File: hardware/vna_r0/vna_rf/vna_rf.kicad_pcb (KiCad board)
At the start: 2 copper layers, 122 parts, among them J401 CONN_02X10, U201 LMX2594, U202 LTC2630, U203 ADRF5040, U204 LTC2054CS5, U205 MAAM-011100, U301 NC7WZU04, U302 PE42521, U303 MASW-008322-TR1000, U304 PE42521, U401 CONN_SMA_2GND, U402 CONN_SMA_2GND, U403 CONN_SMA

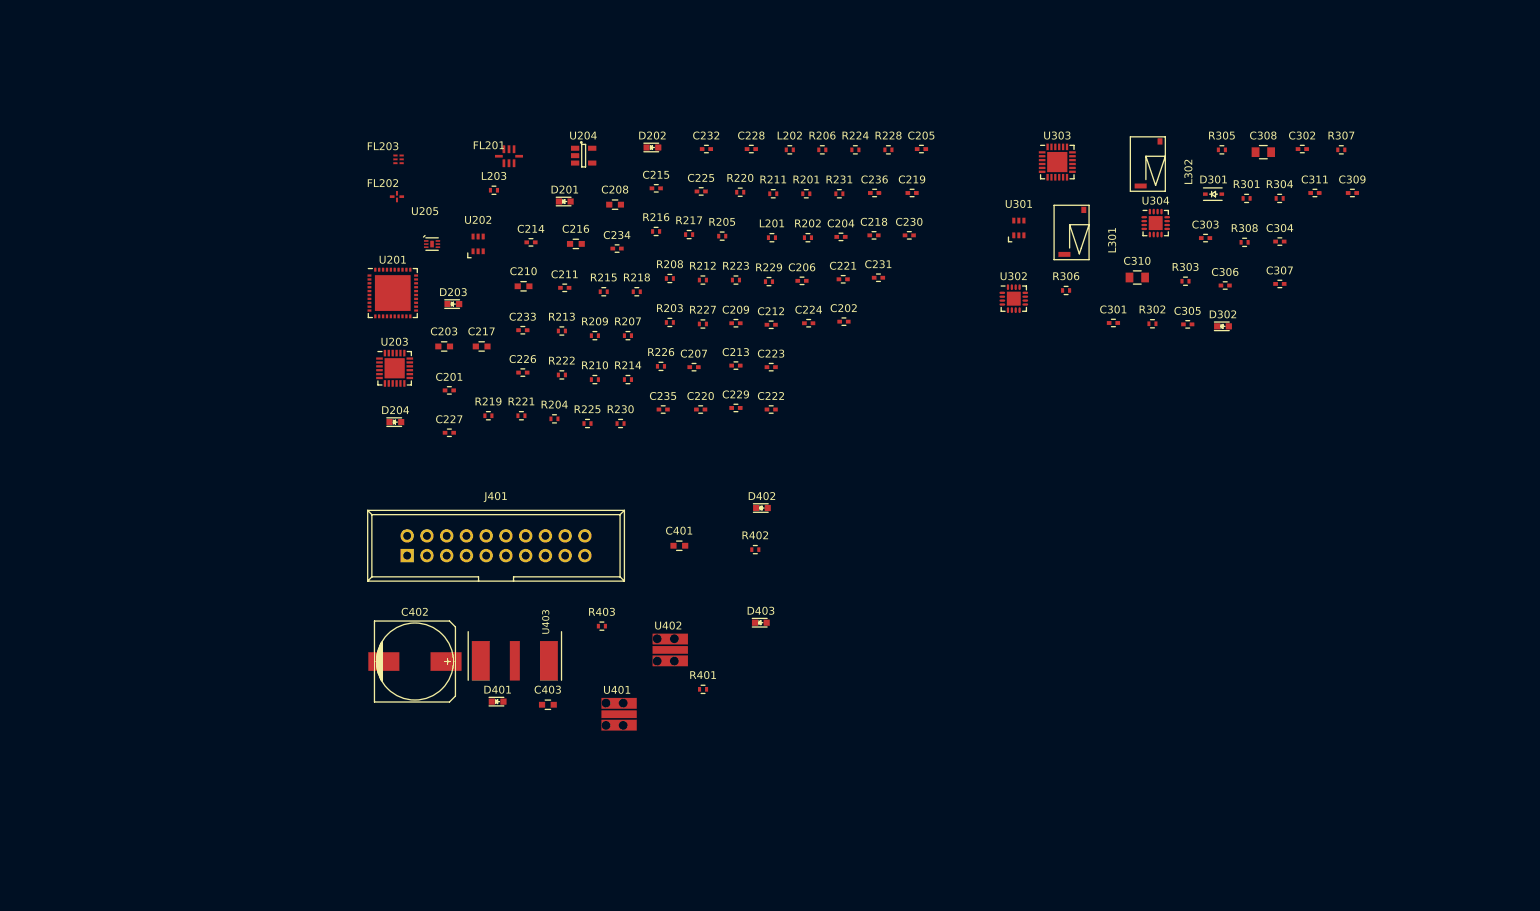
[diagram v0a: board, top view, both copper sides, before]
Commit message: work on vna r0 component placement
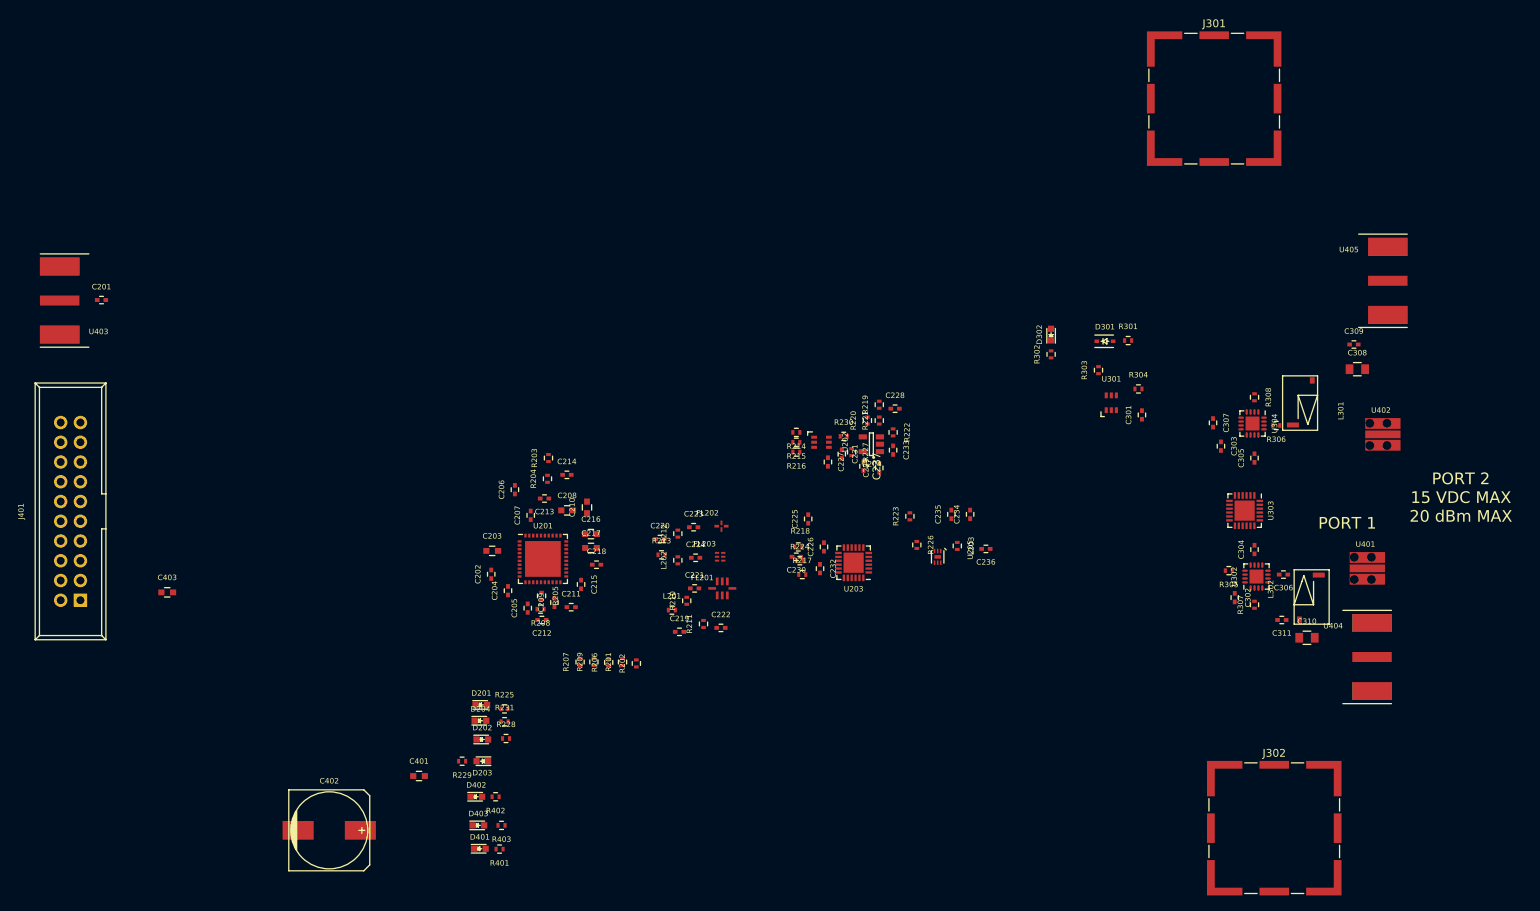
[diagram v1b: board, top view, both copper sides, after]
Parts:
- added C237: 100 nF, Capacitors_SMD:C_0402, F.Cu at (187.5, 95.5)
- added J301: RF_Shield_Two_Pieces, Shielding_Cabinets:Laird_Technologies_BMI-S-202-F_16.50x16.50mm, F.Cu at (232.6, 48.3)
- added J302: RF_Shield_Two_Pieces, Shielding_Cabinets:Laird_Technologies_BMI-S-202-F_16.50x16.50mm, F.Cu at (240.3, 142.1)
- added U404: CONN_SMA, vna_footprints:732511150_sma_thin, F.Cu at (252.9, 120.1)
- added U405: CONN_SMA, vna_footprints:732511150_sma_thin, F.Cu at (254.9, 71.7)
- moved U401 98.0 mm to (252.3, 108.7)
- moved U402 95.8 mm to (254.3, 91.4)
- moved R228 90.3 mm to (141.5, 130.6)
- moved R231 80.4 mm to (141.3, 128.4)
- moved D202 79.2 mm to (138.4, 130.7)
- moved C205 77.8 mm to (144.3, 113.8), turned to 90 degrees
- moved U205 76.5 mm to (197.0, 107.2), turned to 270 degrees
- moved L203 75.1 mm to (199.5, 105.8), turned to 270 degrees
- moved U403 74.7 mm to (84.1, 74.2), turned to 270 degrees
- moved R229 73.2 mm to (135.8, 133.5), turned to 180 degrees
- moved R206 71.4 mm to (154.7, 120.8), turned to 90 degrees
- moved FL203 65.8 mm to (169.0, 107.2)
- moved D201 65.6 mm to (138.3, 126.2)
- moved R201 64.7 mm to (156.5, 120.7), turned to 90 degrees
- moved U203 64.1 mm to (186.2, 108.0), turned to 180 degrees
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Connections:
- net /port_switch/PORT1_BIAS renamed /PORT1_BIAS
- net /port_switch/PORT2_BIAS renamed /PORT2_BIAS
- C304 pad 1: Net-(C304-Pad1) -> /conn_power/PORT1
- R307 pad 1: Net-(R307-Pad1) -> GND
- R307 pad 2: GND -> Net-(R307-Pad2)
- U302 pad 11: Net-(R307-Pad1) -> /conn_power/PORT1
- U302 pad 15: +3V3 -> GND
- U302 pad 2: Net-(C304-Pad1) -> Net-(R307-Pad2)
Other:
- copper layers 2 -> 4
- board text added: "PORT 1"
- board text added: "PORT 2 15 VDC MAX 20 dBm MAX"

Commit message: work on vna r0 layout..
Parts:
- added H401: MOUNTING_HOLE, Mounting_Holes:MountingHole_2-7mm, F.Cu at (192.9, 79.1)
- added H402: MOUNTING_HOLE, Mounting_Holes:MountingHole_2-7mm, F.Cu at (251.0, 120.8)
- added H403: MOUNTING_HOLE, Mounting_Holes:MountingHole_2-7mm, F.Cu at (174.1, 124.1)
- added H404: MOUNTING_HOLE, Mounting_Holes:MountingHole_2-7mm, F.Cu at (251.0, 79.9)
- added J402: RF_Shield_Two_Pieces, Shielding_Cabinets:Laird_Technologies_BMI-S-205-F_38.10x25.40mm, F.Cu at (146.5, 96.6)
- moved U403 92.4 mm to (176.3, 79.2), turned to 180 degrees
- moved C201 87.6 mm to (176.4, 84.6), turned to 270 degrees
- moved J401 85.7 mm to (172.5, 114.3)
- moved C403 81.3 mm to (178.9, 104.6)
- moved C402 75.7 mm to (190.6, 118.5)
- moved D401 62.6 mm to (199.8, 134.2), turned to 90 degrees
- moved R401 60.7 mm to (199.9, 131.6), turned to 270 degrees
- moved D403 59.4 mm to (196.8, 134.3), turned to 90 degrees
- moved C401 58.5 mm to (188.6, 130.6), turned to 90 degrees
- moved R403 56.9 mm to (196.8, 131.4), turned to 270 degrees
- moved D402 55.6 mm to (193.1, 134.6), turned to 90 degrees
- moved D302 53.9 mm to (205.6, 132.2)
- moved R302 53.9 mm to (205.6, 134.7)
- moved R402 53.3 mm to (193.1, 132.1), turned to 270 degrees
- moved R229 52.8 mm to (188.6, 136.4), turned to 270 degrees
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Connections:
- C222 pad 2: /rf_synth/RF_4 -> /rf_synth/RF_1
- C304 pad 1: /conn_power/PORT1 -> Net-(C304-Pad1)
- FL202 pad 3: /rf_synth/RF_1 -> /rf_synth/RF_4
- FL203 pad 3: /rf_synth/RF_2 -> /rf_synth/RF_3
- J401 pad 14: GND -> -5V
- U203 pad 11: (no net) -> /rf_synth/RF_3
- U302 pad 11: /conn_power/PORT1 -> Net-(C305-Pad2)
- U302 pad 15: GND -> +3V3
- U304 pad 11: Net-(C305-Pad2) -> Net-(C304-Pad1)
- U304 pad 15: +3V3 -> GND
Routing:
- net /rf_synth/AMP_VC: track 0.00 -> 14.0 mm
- net /port_switch/SW_V2: track 0.00 -> 10.0 mm
- net GND: track 0.00 -> 9.09 mm, vias 0 -> 10
- net -5V: track 0.00 -> 5.03 mm
- net Net-(C231-Pad1): track 0.00 -> 5.01 mm
- net Net-(C228-Pad1): track 0.00 -> 4.16 mm
- net Net-(D301-Pad2): track 0.00 -> 3.48 mm
- net Net-(R221-Pad1): track 0.00 -> 3.46 mm
- net +3V3: track 0.00 -> 2.81 mm
- net Net-(R216-Pad1): track 0.00 -> 2.19 mm
- net Net-(R214-Pad1): track 0.00 -> 2.19 mm
- net Net-(R304-Pad2): track 0.00 -> 1.90 mm
- net Net-(R215-Pad1): track 0.00 -> 1.84 mm
- net /rf_synth/DAC_VOUT: track 0.00 -> 1.51 mm
- net Net-(R303-Pad2): track 0.00 -> 1.51 mm
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
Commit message: work on demod layout
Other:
- rule pad_to_mask_clearance: 0.2 -> 0.03
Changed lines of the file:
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@@
     (links 421)
     (no_connects 388)
-    (area 0 0 0 0)
+    (area 126.530999 73.1 271.501285 137.986972)
     (thickness 1.6)
     (drawings 2)
@@
   )
   (setup
-    (last_trace_width 0.4)
+    (last_trace_width 0.25)
     (user_trace_width 0.4)
     (trace_clearance 0.2)
@@
     (pad_size 1.524 1.524)
     (pad_drill 0.762)
-    (pad_to_mask_clearance 0.2)
+    (pad_to_mask_clearance 0.03)
     (aux_axis_origin 0 0)
     (visible_elements FFFEFF7F)

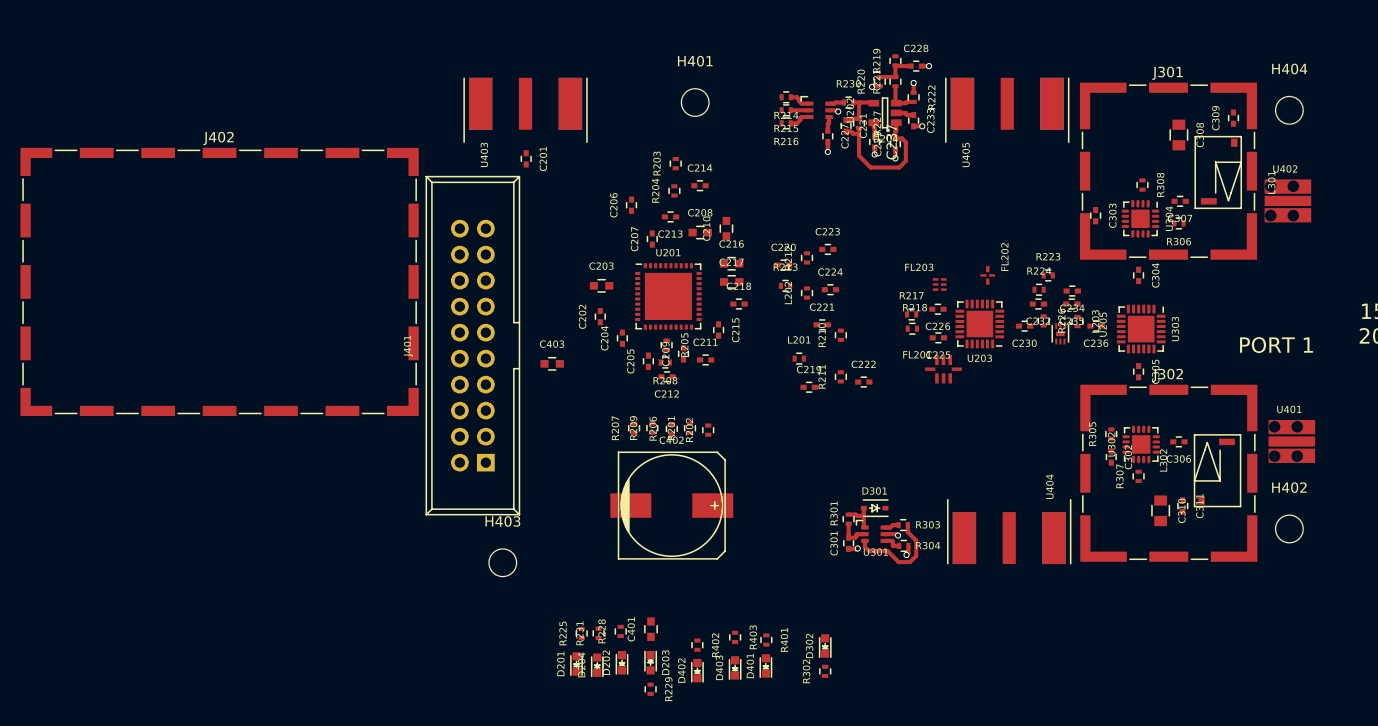
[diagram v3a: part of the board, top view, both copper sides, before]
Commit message: work on vna r0 rf layout
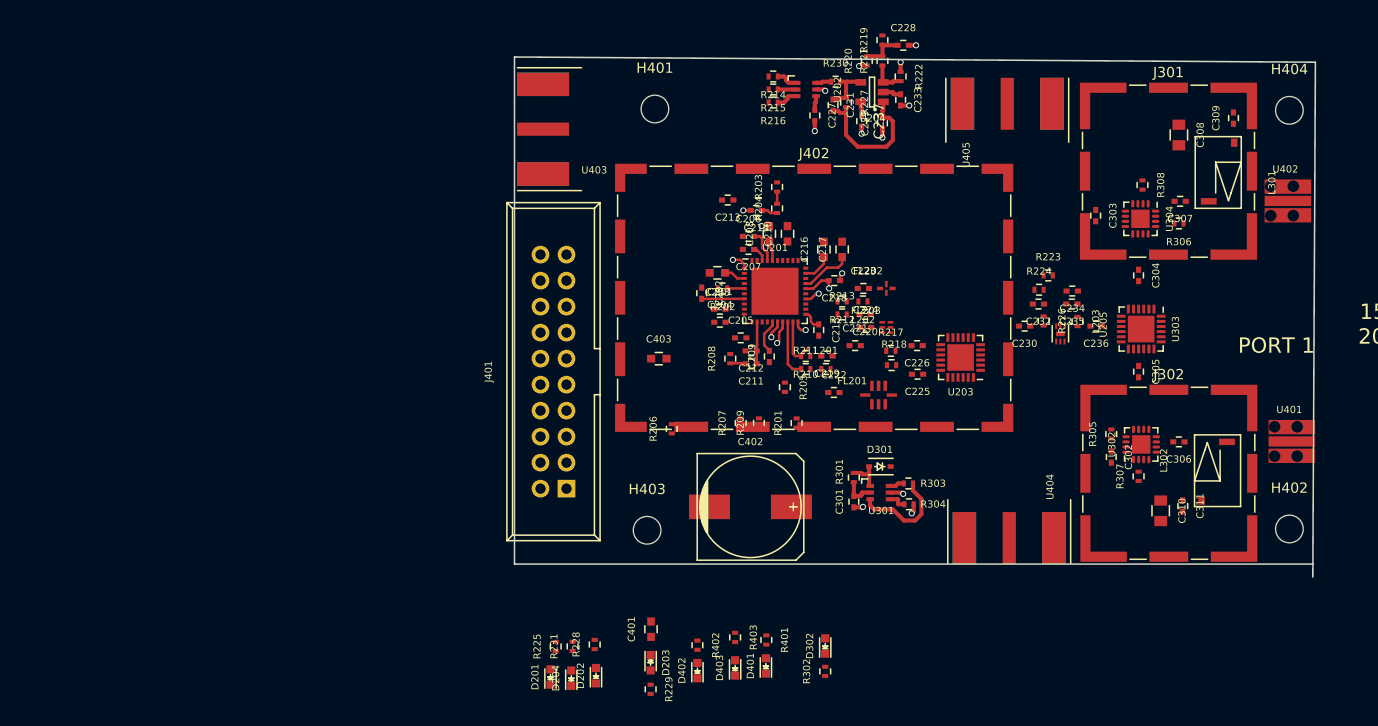
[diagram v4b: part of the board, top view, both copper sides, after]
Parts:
- moved J402 58.1 mm to (204.5, 98.2)
- moved C201 24.0 mm to (195.3, 99.3), turned to 0 degrees
- moved H403 14.5 mm to (188.2, 120.9)
- moved R202 13.9 mm to (195.6, 97.3), turned to 180 degrees
- moved R205 12.3 mm to (201.7, 106.9)
- moved C206 11.8 mm to (198.1, 92.2), turned to 0 degrees
- moved C203 11.4 mm to (195.1, 95.8), turned to 180 degrees
- moved C217 11.2 mm to (207.3, 93.5), turned to 90 degrees
- moved R207 10.4 mm to (197.4, 110.4)
- moved C403 10.4 mm to (189.4, 104.1)
- moved R201 10.4 mm to (202.8, 110.4)
- moved R209 10.4 mm to (199.1, 110.4)
- moved U201 10.4 mm to (200.7, 97.6)
- moved R204 10.2 mm to (200.9, 89.5)
- moved C202 10.2 mm to (193.5, 97.7), turned to 270 degrees
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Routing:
- net +3V3: track 2.81 -> 18.8 mm, vias 0 -> 1
- net /rf_synth/RFOUTBM: track 0.00 -> 5.62 mm
- net /rf_synth/RFOUTBP: track 0.00 -> 5.03 mm
- net Net-(C217-Pad1): track 0.00 -> 5.01 mm
- net /rf_synth/CPOUT: track 0.00 -> 4.11 mm
- net Net-(C216-Pad1): track 0.00 -> 2.81 mm
- net GND: track 9.09 -> 11.4 mm, vias 10 -> 13
- net Net-(R206-Pad1): track 0.00 -> 2.29 mm, vias 0 -> 1
- net Net-(C203-Pad1): track 0.00 -> 2.10 mm
- net Net-(C208-Pad1): track 0.00 -> 1.98 mm
- net Net-(R205-Pad1): track 0.00 -> 1.75 mm, vias 0 -> 1
- net Net-(R202-Pad1): track 0.00 -> 1.69 mm
- net Net-(R201-Pad1): track 0.00 -> 1.69 mm, vias 0 -> 1
- net Net-(C214-Pad1): track 0.00 -> 1.59 mm
- net Net-(C207-Pad1): track 0.00 -> 1.53 mm
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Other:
- board outline added: 78.2 x 50.8 mm

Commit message: work on vna r0 layout
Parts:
- removed D204: LED_Small, LEDs:LED_0603
- removed R231: 1k, Resistors_SMD:R_0402
- added U406: CONN_SMA_2GND, vna_footprints:734120110_ufl_umc, F.Cu at (183.5, 82.0)
- moved R302 56.1 mm to (252.6, 104.0), turned to 180 degrees
- moved D201 55.6 mm to (194.1, 81.8)
- moved R225 55.1 mm to (194.1, 79.2)
- moved C401 54.3 mm to (227.3, 92.5), turned to 180 degrees
- moved D302 52.8 mm to (250.3, 104.0), turned to 180 degrees
- moved R403 39.2 mm to (227.0, 106.5)
- moved D403 39.2 mm to (227.0, 109.5)
- moved R229 22.9 mm to (189.1, 113.5), turned to 90 degrees
- moved D202 19.1 mm to (186.5, 116.3)
- moved R228 19.1 mm to (186.4, 113.3)
- moved D401 18.5 mm to (205.7, 116.6)
- moved R401 18.5 mm to (205.7, 114.1)
- moved D203 17.8 mm to (189.1, 116.1), turned to 90 degrees
- moved D402 17.4 mm to (205.6, 122.4)
- moved R402 17.4 mm to (205.6, 119.9)
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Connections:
- J402 pad 1: Net-(J402-Pad1) -> GND
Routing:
- net /rf_synth/RF_1: track 0.00 -> 18.6 mm
- net /rf_synth/RF_2: track 0.00 -> 11.2 mm
- net Net-(C230-Pad2): track 0.00 -> 6.08 mm
- net -5V: track 5.03 -> 9.39 mm
- net /rf_synth/AMP_VC: track 14.0 -> 11.2 mm
- net /rf_synth/DAC_VOUT: track 1.51 -> 4.06 mm
- net Net-(C228-Pad1): track 4.16 -> 6.34 mm
- net GND: vias 13 -> 12
- net (no net): vias 0 -> 2
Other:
- board size 78.2 x 50.8 mm -> 78 x 49 mm
- board text added: "BIAS IN 1 15V .5A"
- board text added: "BIAS IN 2"
- board text added: "REF IN"
